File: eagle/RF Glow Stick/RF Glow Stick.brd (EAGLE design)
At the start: 25.4 x 49.5 mm, 8 parts, among them J1 GROVE-4P-2.0

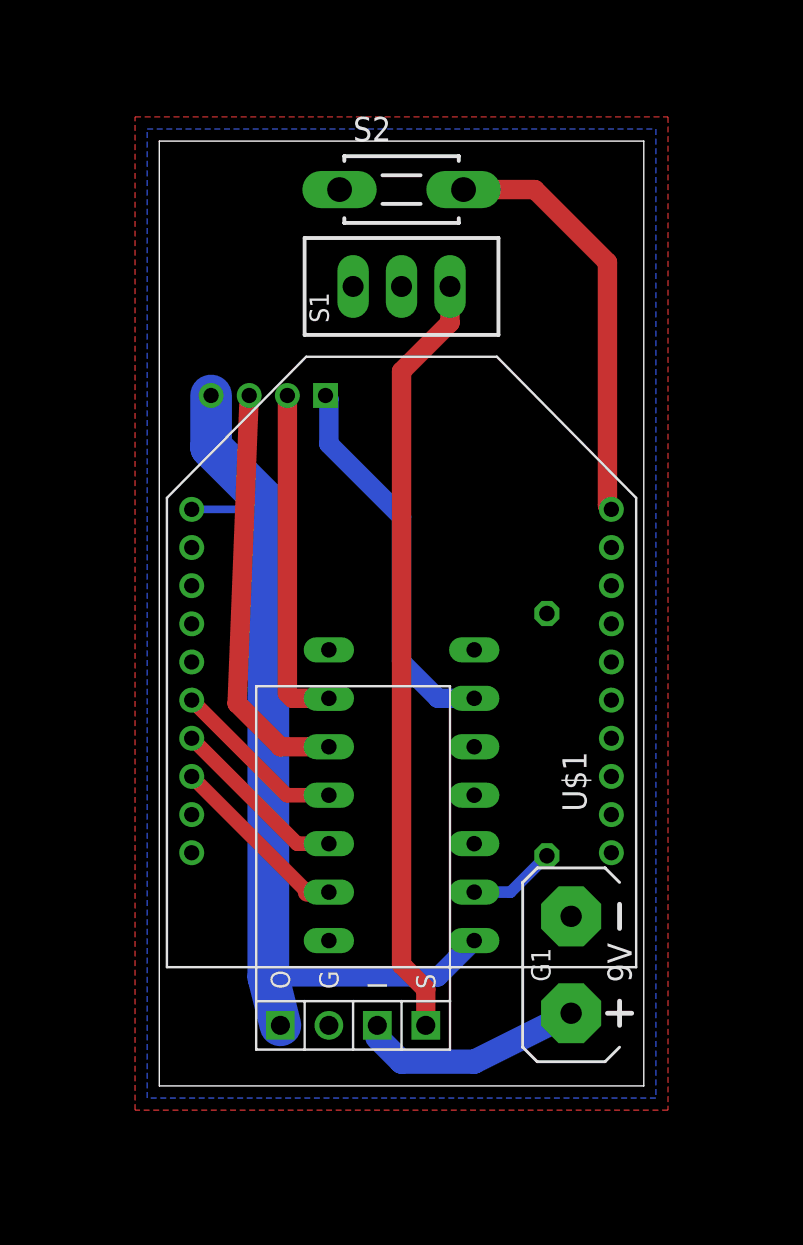
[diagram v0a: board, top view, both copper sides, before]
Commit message: Fixed flawed board design. The LED connector needs to be in the middle to clear the PCB holding ledges and to have maximum clearance for round handles. Also reduced the side of the board from 5.08cm long (2 inches) to 4.99cm for cheaper Fusion PCB pricing.
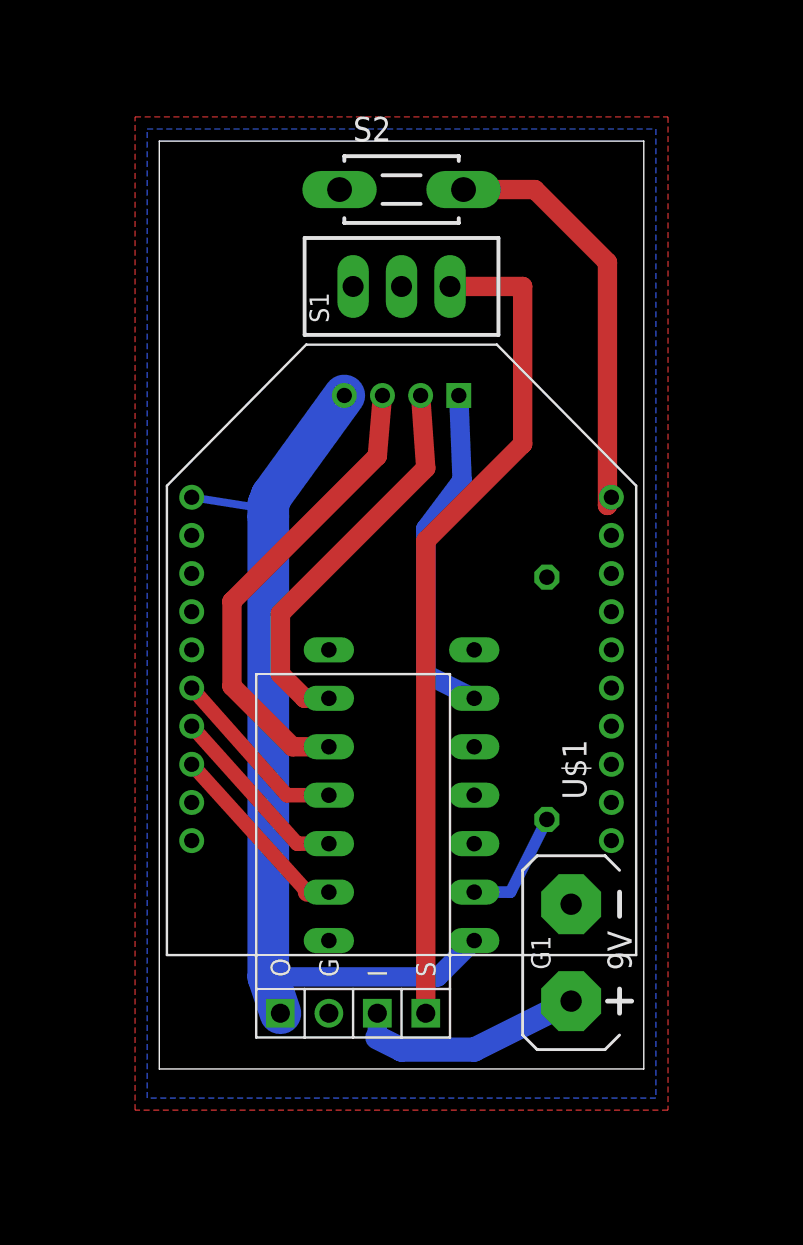
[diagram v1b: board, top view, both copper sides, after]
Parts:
- moved J1 6.98 mm to (12.7, 36.2)
- moved R1 1.91 mm to (20.3, 20.3)
- moved G1 0.64 mm to (21.6, 6.99)
- moved MOD1 0.63 mm to (10.2, 12.7)
- moved U$1 0.63 mm to (12.7, 22.9)
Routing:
- net N$2: track 40.3 -> 44.0 mm
- net N$9: track 17.9 -> 20.8 mm
- net N$1: track 21.9 -> 24.8 mm
- net N$10: track 20.2 -> 18.1 mm
- net N$11: track 4.60 -> 6.16 mm
- net VOUT: track 51.1 -> 50.5 mm
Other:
- board size 25.4 x 49.5 mm -> 25.4 x 48.6 mm
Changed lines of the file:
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@@
 <grid distance="0.025" unitdist="inch" unit="inch" style="lines" multiple="1" display="yes" altdistance="0.0125" altunitdist="inch" altunit="inch"/>
 <layers>
-<layer number="1" name="Top" color="4" fill="1" visible="yes" active="yes"/>
+<layer number="1" name="Top" color="4" fill="1" visible="no" active="yes"/>
 <layer number="16" name="Bottom" color="1" fill="1" visible="yes" active="yes"/>
 <layer number="17" name="Pads" color="2" fill="1" visible="yes" active="yes"/>
@@
 <board>
 <plain>
-<wire x1="0" y1="0" x2="25.4" y2="0" width="0" layer="20"/>
-<wire x1="25.4" y1="0" x2="25.4" y2="49.53" width="0" layer="20"/>
+<wire x1="0" y1="0.889" x2="25.4" y2="0.889" width="0" layer="20"/>
+<wire x1="25.4" y1="0.889" x2="25.4" y2="49.53" width="0" layer="20"/>
 <wire x1="25.4" y1="49.53" x2="0" y2="49.53" width="0" layer="20"/>
-<wire x1="0" y1="49.53" x2="0" y2="0" width="0" layer="20"/>
+<wire x1="0" y1="49.53" x2="0" y2="0.889" width="0" layer="20"/>
 </plain>
 <attributes>
@@
 </autorouter>
 <elements>
-<element name="MOD1" library="My Library" package="POLOLU_REG09B" value="POLOLU" x="10.16" y="12.065"/>
-<element name="U$1" library="My Library" package="RFBEE" value="RFBEE1.11.1" x="12.7" y="22.225"/>
+<element name="MOD1" library="My Library" package="POLOLU_REG09B" value="POLOLU" x="10.16" y="12.7"/>
+<element name="U$1" library="My Library" package="RFBEE" value="RFBEE1.11.1" x="12.7" y="22.86"/>
 <element name="U$2" library="My Library" package="DIL14" value="STP04CM05" x="12.7" y="15.24" rot="MR90"/>
 <element name="S1" library="switch" package="TL3XPO" value="" x="12.7" y="41.91" smashed="yes">
@@
 <attribute name="VALUE" x="7.62" y="36.83" size="1.778" layer="27"/>
 </element>
-<element name="G1" library="battery" package="AB9V" value="" x="21.59" y="6.35" smashed="yes" rot="R180">
-<attribute name="NAME" x="20.0025" y="6.35" size="1.016" layer="25" ratio="10" rot="R270" align="center"/>
-<attribute name="VALUE" x="17.145" y="8.89" size="1.27" layer="27" ratio="10" rot="R270"/>
+<element name="G1" library="battery" package="AB9V" value="" x="21.59" y="6.985" smashed="yes" rot="R180">
+<attribute name="NAME" x="20.0025" y="6.985" size="1.016" layer="25" ratio="10" rot="R270" align="center"/>
+<attribute name="VALUE" x="17.145" y="9.525" size="1.27" layer="27" ratio="10" rot="R270"/>
 </element>
-<element name="J1" library="My Library" package="4P-2.0-90D" value="GROVE-4P-2.0" x="5.715" y="36.195" rot="MR0"/>
+<element name="J1" library="My Library" package="4P-2.0-90D" value="GROVE-4P-2.0" x="12.7" y="36.195" rot="MR0"/>
 <element name="S2" library="switch-tact" package="DTS-3" value="DTS-3" x="12.7" y="46.99"/>
-<element name="R1" library="rcl" package="0309/12" value="200" x="20.32" y="18.415" rot="MR270"/>
+<element name="R1" library="rcl" package="0309/12" value="200" x="20.32" y="20.32" rot="MR270"/>
 </elements>
 <signals>
@@
 <contactref element="MOD1" pad="I"/>
 <contactref element="G1" pad="+"/>
-<wire x1="21.59" y1="3.81" x2="16.51" y2="1.27" width="1.27" layer="16"/>
-<wire x1="16.51" y1="1.27" x2="12.7" y2="1.27" width="1.27" layer="16"/>
-<wire x1="12.7" y1="1.27" x2="11.43" y2="2.54" width="1.27" layer="16"/>
-<wire x1="11.43" y1="2.54" x2="11.43" y2="3.175" width="1.016" layer="16"/>
+<wire x1="21.59" y1="4.445" x2="16.51" y2="1.905" width="1.27" layer="16"/>
+<wire x1="16.51" y1="1.905" x2="12.7" y2="1.905" width="1.27" layer="16"/>
+<wire x1="12.7" y1="1.905" x2="11.43" y2="2.54" width="1.27" layer="16"/>
+<wire x1="11.43" y1="2.54" x2="11.43" y2="3.81" width="1.016" layer="16"/>
 </signal>
 <signal name="GND">
@@
 <contactref element="MOD1" pad="S"/>
 <contactref element="S1" pad="3"/>
-<wire x1="15.24" y1="41.91" x2="15.24" y2="40.005" width="1.016" layer="1"/>
-<wire x1="15.24" y1="40.005" x2="12.7" y2="37.465" width="1.016" layer="1"/>
-<wire x1="12.7" y1="37.465" x2="12.7" y2="6.35" width="1.016" layer="1"/>
-<wire x1="13.97" y1="3.175" x2="13.97" y2="5.08" width="1.016" layer="1"/>
-<wire x1="13.97" y1="5.08" x2="12.7" y2="6.35" width="1.016" layer="1"/>
+<wire x1="13.97" y1="3.81" x2="13.97" y2="28.575" width="1.016" layer="1"/>
+<wire x1="13.97" y1="28.575" x2="19.05" y2="33.655" width="1.016" layer="1"/>
+<wire x1="19.05" y1="33.655" x2="19.05" y2="41.91" width="1.016" layer="1"/>
+<wire x1="19.05" y1="41.91" x2="15.24" y2="41.91" width="1.016" layer="1"/>
 </signal>
 <signal name="VOUT">
@@
 <contactref element="U$1" pad="P$1"/>
 <contactref element="J1" pad="BLACK"/>
-<wire x1="6.35" y1="3.175" x2="5.715" y2="5.715" width="2.1844" layer="16"/>
+<wire x1="6.35" y1="3.81" x2="5.715" y2="5.715" width="2.1844" layer="16"/>
 <wire x1="5.715" y1="5.715" x2="5.715" y2="29.845" width="2.1844" layer="16"/>
 <wire x1="6.35" y1="30.225" x2="5.715" y2="29.845" width="0.4064" layer="16"/>
@@
 <wire x1="16.51" y1="7.62" x2="14.605" y2="5.715" width="1.016" layer="16"/>
 <wire x1="14.605" y1="5.715" x2="5.715" y2="5.715" width="1.016" layer="16"/>
-<wire x1="1.7" y1="30.225" x2="5.715" y2="30.225" width="0.4064" layer="16"/>
+<wire x1="1.7" y1="30.86" x2="5.715" y2="30.225" width="0.4064" layer="16"/>
 <wire x1="5.715" y1="30.225" x2="5.715" y2="29.845" width="0.4064" layer="16"/>
 <wire x1="5.715" y1="29.845" x2="5.715" y2="30.48" width="2.1844" layer="16"/>
-<wire x1="2.715" y1="36.195" x2="2.715" y2="33.48" width="2.1844" layer="16"/>
-<wire x1="2.715" y1="33.48" x2="5.715" y2="30.48" width="2.1844" layer="16"/>
+<wire x1="9.7" y1="36.195" x2="5.89" y2="30.94" width="2.1844" layer="16"/>
+<wire x1="5.89" y1="30.94" x2="5.715" y2="30.48" width="2.1844" layer="16"/>
 </signal>
 <signal name="N$5">
@@
 <contactref element="U$2" pad="4"/>
 <wire x1="8.89" y1="15.24" x2="6.685" y2="15.24" width="0.762" layer="1"/>
-<wire x1="6.685" y1="15.24" x2="1.7" y2="20.225" width="0.762" layer="1"/>
+<wire x1="6.685" y1="15.24" x2="1.7" y2="20.86" width="0.762" layer="1"/>
 </signal>
 <signal name="N$6">
@@
 <contactref element="U$2" pad="3"/>
 <wire x1="8.89" y1="12.7" x2="7.225" y2="12.7" width="0.762" layer="1"/>
-<wire x1="7.225" y1="12.7" x2="1.7" y2="18.225" width="0.762" layer="1"/>
+<wire x1="7.225" y1="12.7" x2="1.7" y2="18.86" width="0.762" layer="1"/>
 </signal>
 <signal name="N$7">
 <contactref element="U$1" pad="P$8"/>
 <contactref element="U$2" pad="2"/>
-<wire x1="1.7" y1="16.225" x2="7.765" y2="10.16" width="0.762" layer="1"/>
+<wire x1="1.7" y1="16.86" x2="7.765" y2="10.16" width="0.762" layer="1"/>
 <wire x1="7.765" y1="10.16" x2="8.89" y2="10.16" width="1.016" layer="1"/>
 </signal>
@@
 <contactref element="U$2" pad="5"/>
 <contactref element="J1" pad="RED"/>
-<wire x1="4.715" y1="36.195" x2="4.08" y2="20.05" width="1.016" layer="1"/>
-<wire x1="4.08" y1="20.05" x2="6.35" y2="17.78" width="1.016" layer="1"/>
-<wire x1="6.35" y1="17.78" x2="8.89" y2="17.78" width="1.016" layer="1"/>
+<wire x1="8.89" y1="17.78" x2="6.985" y2="17.78" width="1.016" layer="1"/>
+<wire x1="6.985" y1="17.78" x2="3.81" y2="20.955" width="1.016" layer="1"/>
+<wire x1="3.81" y1="20.955" x2="3.81" y2="25.4" width="1.016" layer="1"/>
+<wire x1="3.81" y1="25.4" x2="11.43" y2="33.02" width="1.016" layer="1"/>
+<wire x1="11.43" y1="33.02" x2="11.7" y2="36.195" width="1.016" layer="1"/>
 </signal>
 <signal name="N$11">
@@
 <contactref element="R1" pad="2"/>
 <wire x1="16.51" y1="10.16" x2="18.415" y2="10.16" width="0.6096" layer="16"/>
-<wire x1="18.415" y1="10.16" x2="20.32" y2="12.065" width="0.6096" layer="16"/>
+<wire x1="18.415" y1="10.16" x2="20.32" y2="13.97" width="0.6096" layer="16"/>
 </signal>
 <signal name="N$9">
 <contactref element="U$2" pad="6"/>
 <contactref element="J1" pad="WHITE"/>
-<wire x1="6.715" y1="36.195" x2="6.715" y2="20.59" width="1.016" layer="1"/>
-<wire x1="6.715" y1="20.59" x2="6.985" y2="20.32" width="1.016" layer="1"/>
-<wire x1="6.985" y1="20.32" x2="8.89" y2="20.32" width="1.016" layer="1"/>
+<wire x1="8.89" y1="20.32" x2="7.62" y2="20.32" width="1.016" layer="1"/>
+<wire x1="7.62" y1="20.32" x2="6.35" y2="21.59" width="1.016" layer="1"/>
+<wire x1="6.35" y1="21.59" x2="6.35" y2="24.765" width="1.016" layer="1"/>
+<wire x1="6.35" y1="24.765" x2="13.97" y2="32.385" width="1.016" layer="1"/>
+<wire x1="13.97" y1="32.385" x2="13.7" y2="36.195" width="1.016" layer="1"/>
 </signal>
 <signal name="N$10">
 <contactref element="U$2" pad="9"/>
 <contactref element="J1" pad="YELLOW"/>
-<wire x1="16.51" y1="20.32" x2="14.605" y2="20.32" width="1.016" layer="16"/>
-<wire x1="14.605" y1="20.32" x2="12.7" y2="22.225" width="1.016" layer="16"/>
-<wire x1="12.7" y1="22.225" x2="12.7" y2="29.845" width="1.016" layer="16"/>
-<wire x1="12.7" y1="29.845" x2="8.89" y2="33.655" width="1.016" layer="16"/>
-<wire x1="8.89" y1="33.655" x2="8.89" y2="36.02" width="1.016" layer="16"/>
-<wire x1="8.89" y1="36.02" x2="8.715" y2="36.195" width="1.016" layer="16"/>
+<wire x1="16.51" y1="20.32" x2="13.97" y2="21.59" width="1.016" layer="16"/>
+<wire x1="13.97" y1="21.59" x2="13.97" y2="29.21" width="1.016" layer="16"/>
+<wire x1="13.97" y1="29.21" x2="15.875" y2="31.75" width="1.016" layer="16"/>
+<wire x1="15.875" y1="31.75" x2="15.7" y2="36.195" width="1.016" layer="16"/>
 </signal>
 <signal name="N$3">
@@
 <wire x1="19.685" y1="46.99" x2="23.495" y2="43.18" width="1.016" layer="1"/>
 <wire x1="23.495" y1="43.18" x2="23.495" y2="30.43" width="1.016" layer="1"/>
-<wire x1="23.495" y1="30.43" x2="23.7" y2="30.225" width="1.016" layer="1"/>
+<wire x1="23.495" y1="30.43" x2="23.7" y2="30.86" width="1.016" layer="1"/>
 </signal>
 </signals>

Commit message: Updated board to be compatible with milling fabrication (e.g. a CNC mill with an engraving tool for isolation routing). However, actual isolution routed board is nonfunctional because the design relies upon through-plated holes to connect the top and bottom traces.
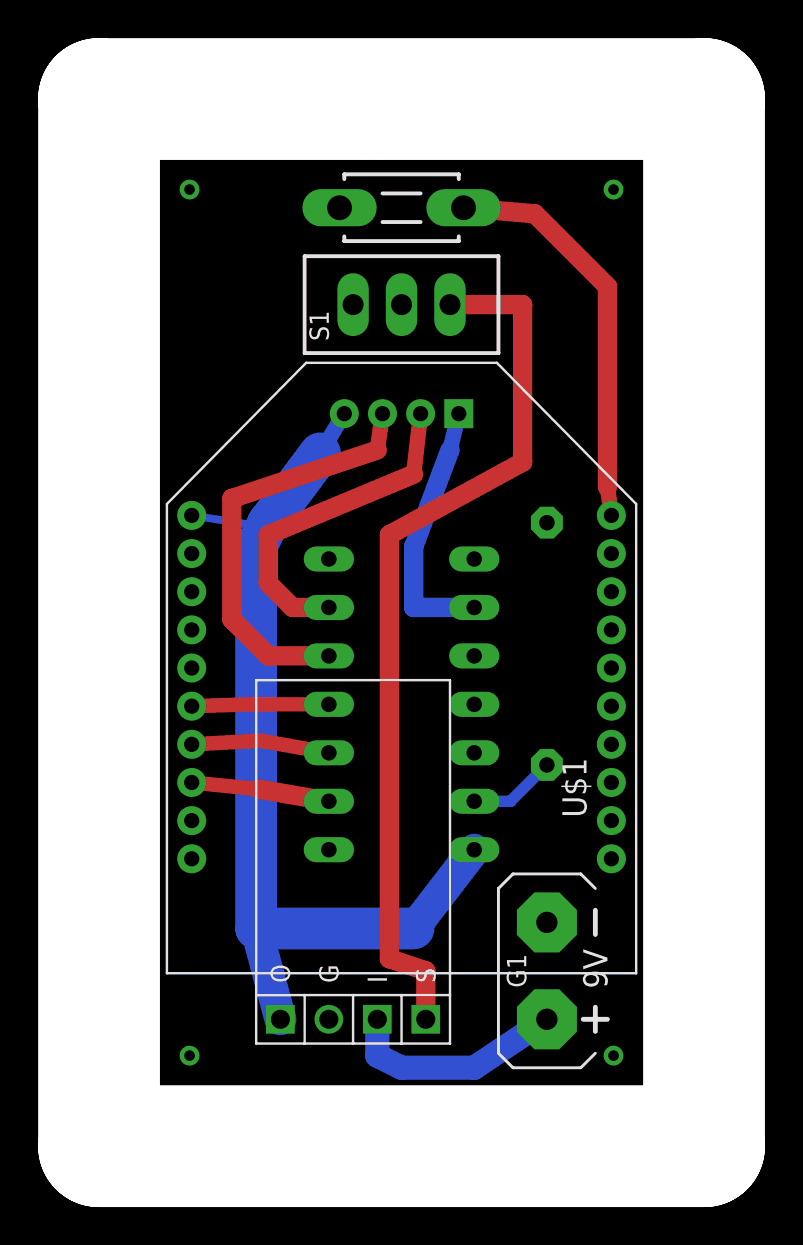
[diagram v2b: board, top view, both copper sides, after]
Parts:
- S1: value (none) -> TL32PO
- moved U$2 4.76 mm to (12.7, 20.0)
- moved R1 2.86 mm to (20.3, 23.2)
- moved G1 1.59 mm to (20.3, 6.03)
- moved J1 0.95 mm to (12.7, 35.2)
- moved S2 0.95 mm to (12.7, 46.0)
- moved U$1 0.95 mm to (12.7, 21.9)
- moved S1 0.95 mm to (12.7, 41.0)
- moved MOD1 0.32 mm to (10.2, 12.4)
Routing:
- net N$10: track 18.1 -> 13.7 mm
- net VOUT: track 50.5 -> 53.7 mm
- net N$9: track 20.8 -> 17.7 mm
- net N$7: track 10.2 -> 7.26 mm
- net N$2: track 44.0 -> 46.8 mm
- net N$6: track 9.94 -> 7.25 mm
- net N$1: track 24.8 -> 22.2 mm
- net N$5: track 9.72 -> 7.19 mm
- net N$11: track 6.16 -> 4.60 mm
- net N$3: track 22.3 -> 21.2 mm
- net GND: track 0.63 -> 0.00 mm, vias 0 -> 4
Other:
- board size 25.4 x 48.6 mm -> 31.8 x 54.9 mm
